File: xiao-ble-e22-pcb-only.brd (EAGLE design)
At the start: 40.4 x 55.2 mm, 6 parts, among them U1 XIAO-NRF52840/SENSEXIAO-NRF52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, U2 E22-900M30S

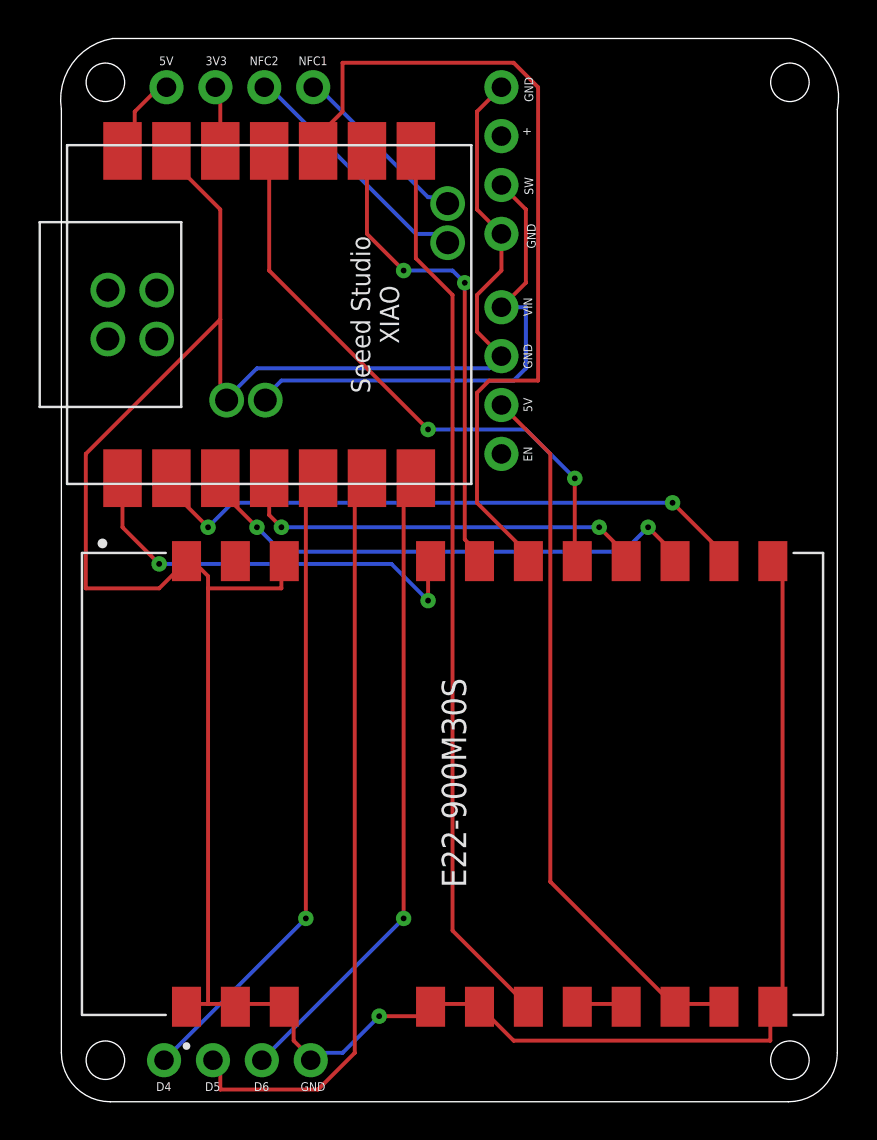
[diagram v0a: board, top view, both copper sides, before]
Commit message: Fix issues with board (spacing between XIAO and MiniBoost, MISO/MOSI swapperoo), break out debug pins, reroute
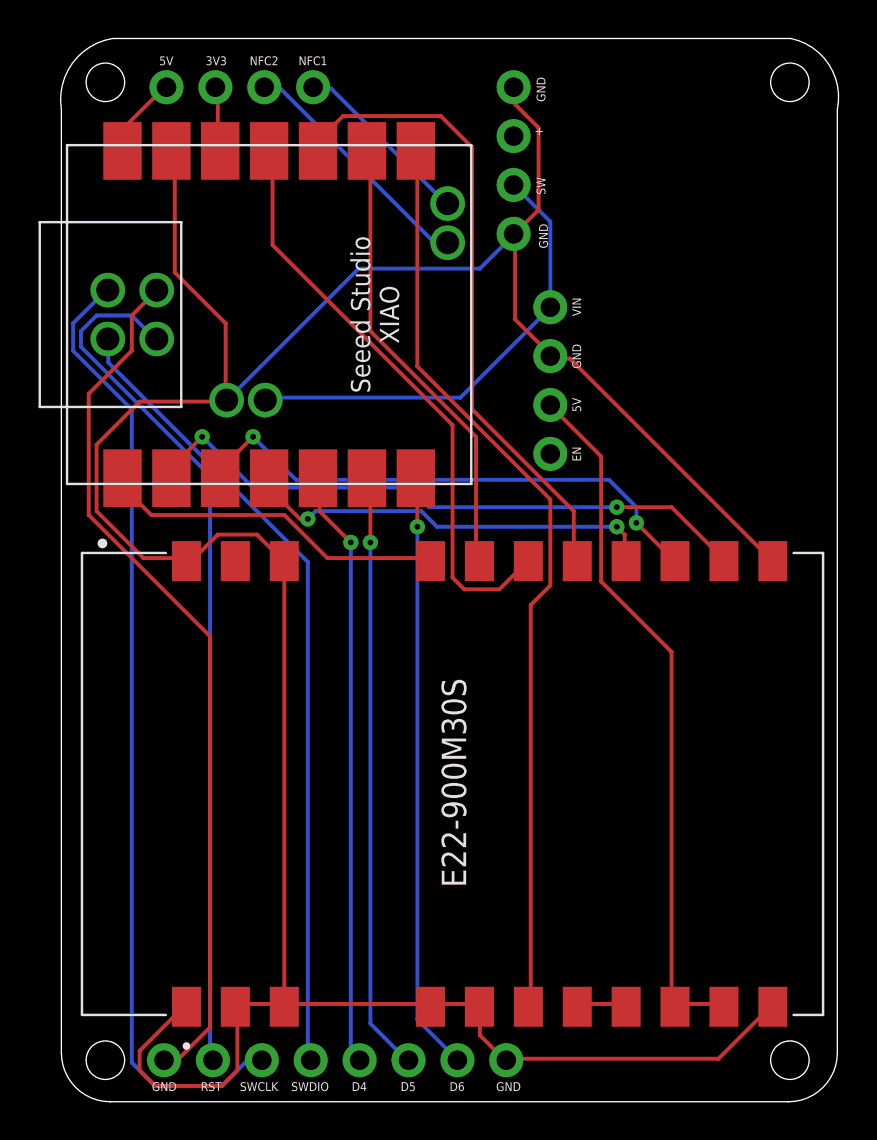
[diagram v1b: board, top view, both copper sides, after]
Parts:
- added JP5: GPIO Breakout 2, breakouts:PADS-4
- moved JP3 10.2 mm to (19.3, 2.16)
- moved JP1 2.54 mm to (25.4, 37.5)
- moved JP4 0.64 mm to (23.5, 48.9)
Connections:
- new net N$14: JP5.1, U1.18
- new net N$17: JP5.2, U1.17
- new net N$21: JP5.3, U1.16
- new net N$22: JP5.4, U1.15
- net N$8: now also U1.10; no longer U1.11
- net N$9: now also U1.11; no longer U1.10
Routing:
- net N$21: track 0.00 -> 50.0 mm
- net N$17: track 0.00 -> 45.5 mm
- net N$14: track 0.00 -> 45.4 mm
- net N$22: track 0.00 -> 41.9 mm
- net N$9: track 44.3 -> 31.0 mm
- net N$19: track 39.6 -> 31.2 mm, vias 0 -> 1
- net N$6: track 22.1 -> 18.1 mm, vias 2 -> 0
- net N$8: track 30.9 -> 33.5 mm, vias 2 -> 0
- net N$18: track 33.5 -> 31.1 mm
- net N$20: track 33.5 -> 31.1 mm
- net N$13: track 26.1 -> 23.9 mm
- net GND: track 157.3 -> 155.8 mm, vias 1 -> 0
- net N$7: track 25.2 -> 23.8 mm, vias 2 -> 0
- net N$4: track 46.9 -> 47.8 mm
- net N$1: track 37.6 -> 36.7 mm
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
